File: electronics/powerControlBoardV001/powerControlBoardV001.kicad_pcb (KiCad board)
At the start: 2 copper layers, 2 parts

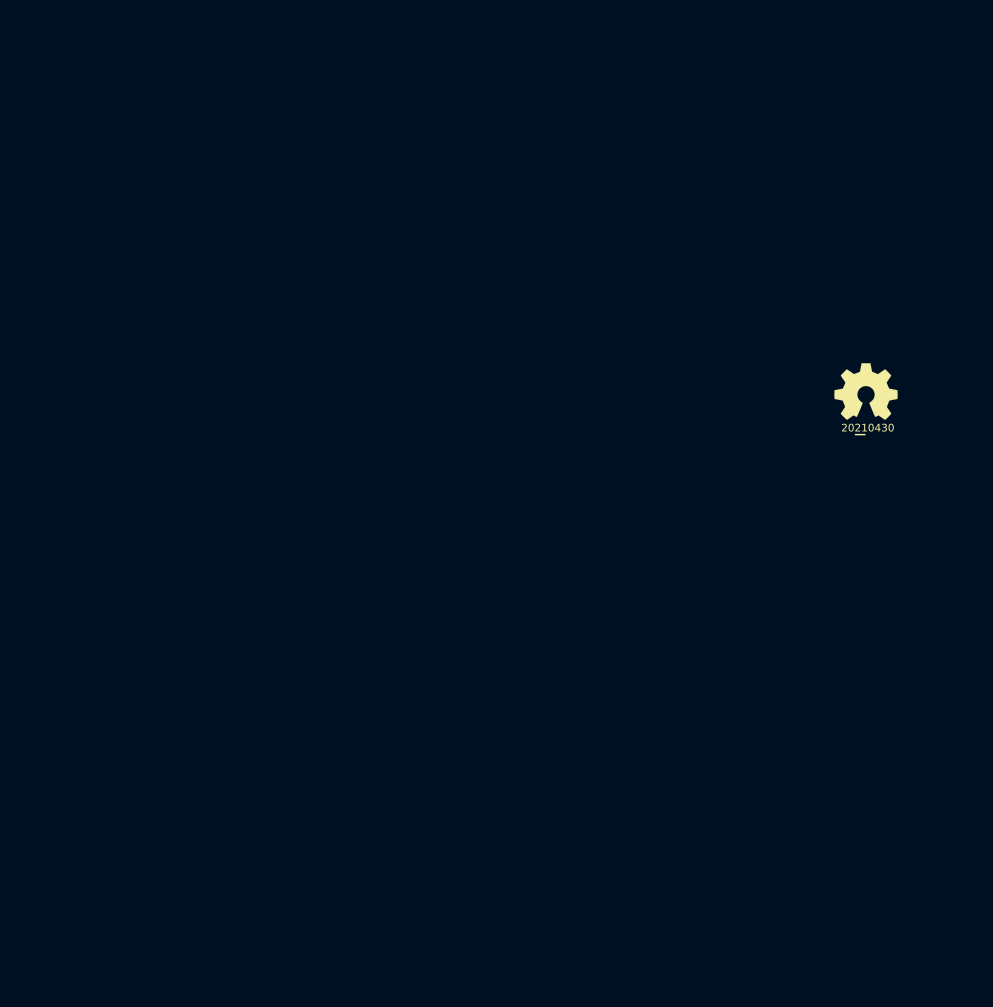
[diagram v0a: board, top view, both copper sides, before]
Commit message: created initial schematic and connections and first PCB outline
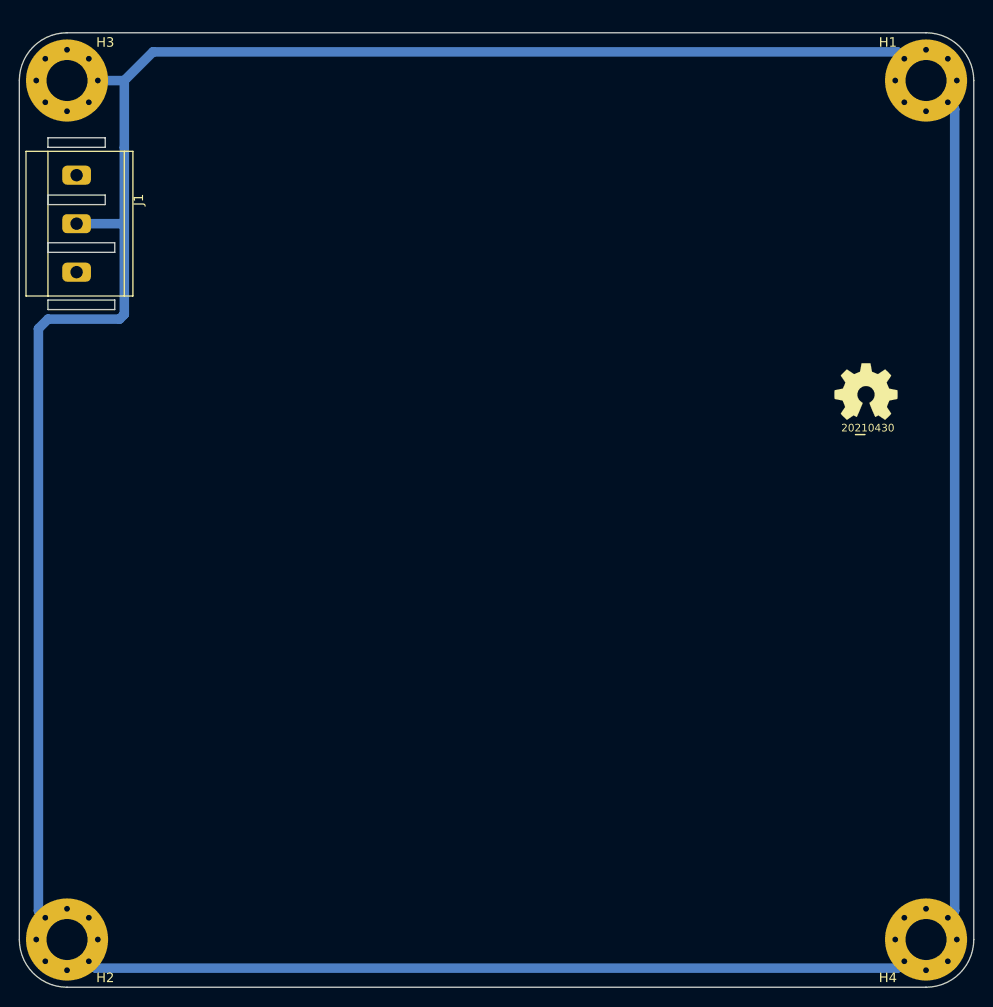
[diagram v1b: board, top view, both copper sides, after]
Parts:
- added H1: M4, MountingHole:MountingHole_4.3mm_M4_Pad_Via, F.Cu at (145.0, 55.0)
- added H2: M4, MountingHole:MountingHole_4.3mm_M4_Pad_Via, F.Cu at (55.0, 145.0)
- added H3: M4, MountingHole:MountingHole_4.3mm_M4_Pad_Via, F.Cu at (55.0, 55.0)
- added H4: M4, MountingHole:MountingHole_4.3mm_M4_Pad_Via, F.Cu at (145.0, 145.0)
- added J1: Conn_01x03, SquantorPhoenixContact:MKDS_3conn_508pitch_1711725, F.Cu at (56.0, 70.0)
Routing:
- net Earth: track 0.00 -> 381.8 mm
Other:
- board outline added: 100 x 100 mm

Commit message: added net filtering parts to PCB, placed, routed, silk optimized
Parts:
- added C201: 4.7n Y2, Capacitor_THT:C_Disc_D10.5mm_W5.0mm_P7.50mm, F.Cu at (84.0, 68.0)
- added C202: 4.7n Y2, Capacitor_THT:C_Disc_D10.5mm_W5.0mm_P7.50mm, F.Cu at (73.0, 68.0)
- added C203: 100n X2, Capacitor_THT:C_Rect_L13.0mm_W6.0mm_P10.00mm_FKS3_FKP3_MKS4, F.Cu at (80.0, 74.0)
- added F201: Fuse, Fuse:Fuseholder_Cylinder-5x20mm_Stelvio-Kontek_PTF78_Horizontal_Open, F.Cu at (87.0, 58.0)
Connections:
- J1 pad 1: /Line -> /Line_in
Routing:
- net /Neutral: track 0.00 -> 42.5 mm
- net Earth: track 381.8 -> 400.7 mm
- net /Line_out: track 0.00 -> 18.9 mm
- net /Line_in: track 0.00 -> 12.8 mm

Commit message: updated versionnumber and cleanup of parts, WIP overall architecture
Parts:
- removed C201, C202: 4.7n Y2, Capacitor_THT:C_Disc_D10.5mm_W5.0mm_P7.50mm
- removed C203: 100n X2, Capacitor_THT:C_Rect_L13.0mm_W6.0mm_P10.00mm_FKS3_FKP3_MKS4
- removed F201: Fuse, Fuse:Fuseholder_Cylinder-5x20mm_Stelvio-Kontek_PTF78_Horizontal_Open
- N1: value 20210430 -> 20220427
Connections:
- J1 pad 1: /Line_in -> /L_in
- J1 pad 3: /Neutral -> /N_in
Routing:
- net Earth: track 400.7 -> 0.00 mm
- net /Neutral: track 42.5 -> 0.00 mm
- net /Line_out: track 18.9 -> 0.00 mm
- net /Line_in: track 12.8 -> 0.00 mm

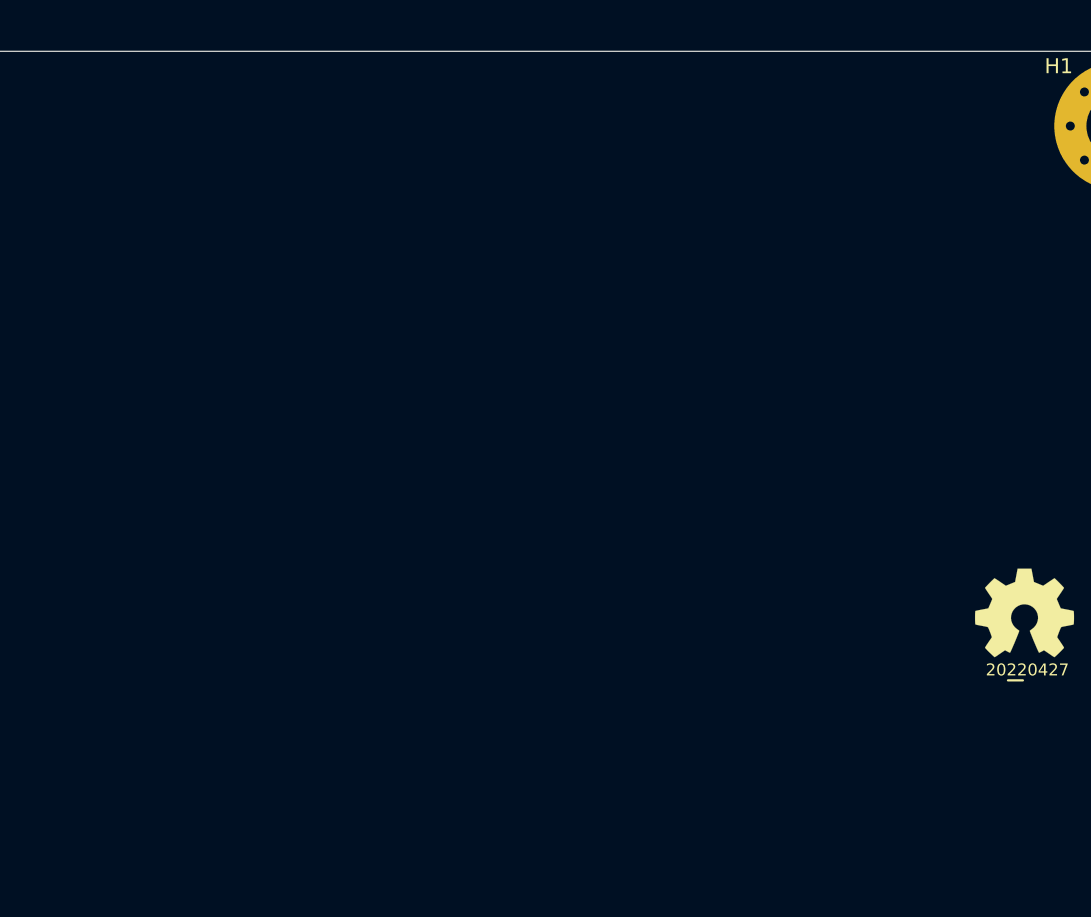
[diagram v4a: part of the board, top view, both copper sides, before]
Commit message: imported initial components into PCB
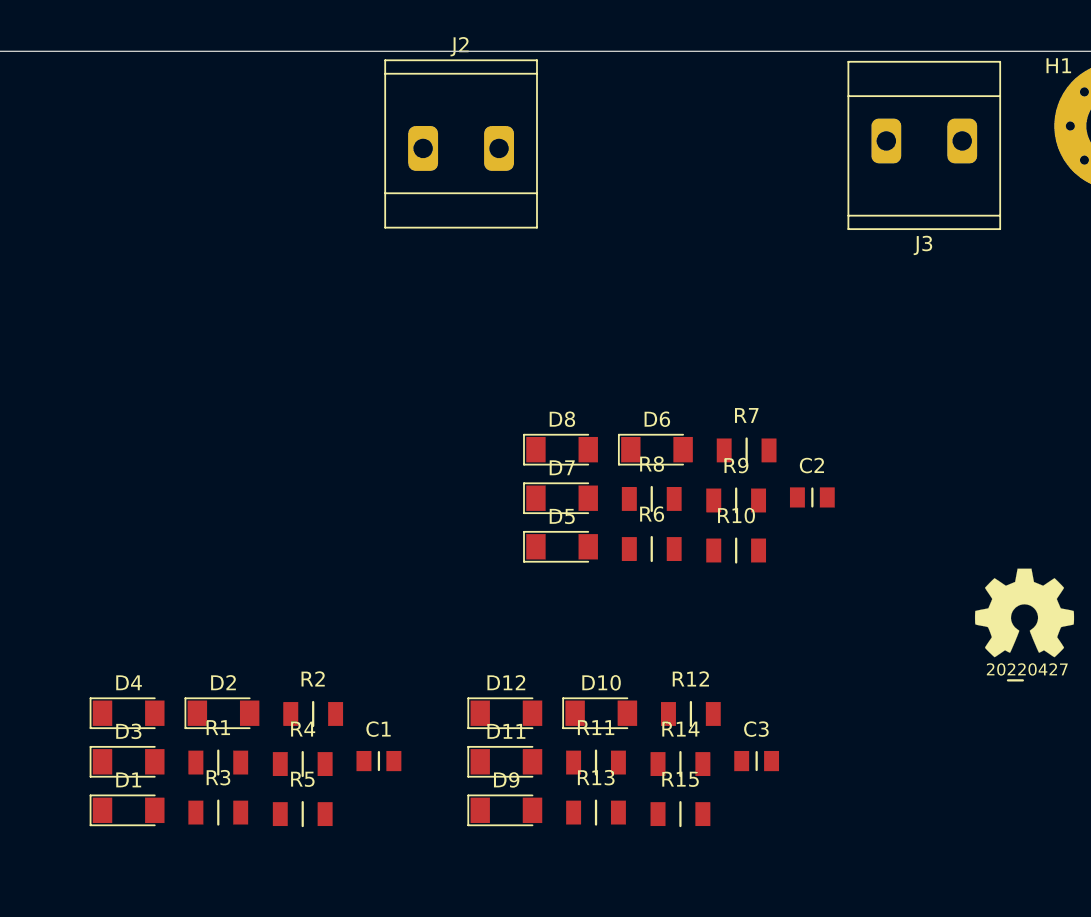
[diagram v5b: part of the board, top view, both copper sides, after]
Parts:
- added C1: 10n, SquantorRcl:C_0805, F.Cu at (95.5, 97.5)
- added C2: 10n, SquantorRcl:C_0805, F.Cu at (124.5, 79.9)
- added C3: 10n, SquantorRcl:C_0805, F.Cu at (120.8, 97.5)
- added D1: 1N4148, Diode_SMD:D_MiniMELF, F.Cu at (78.8, 100.8)
- added D10: 1N4148, Diode_SMD:D_MiniMELF, F.Cu at (110.4, 94.3)
- added D11: 1N4148, Diode_SMD:D_MiniMELF, F.Cu at (104.0, 97.5)
- added D12: 1N4148, Diode_SMD:D_MiniMELF, F.Cu at (104.0, 94.3)
- added D2: 1N4148, Diode_SMD:D_MiniMELF, F.Cu at (85.1, 94.3)
- added D3: 1N4148, Diode_SMD:D_MiniMELF, F.Cu at (78.8, 97.5)
- added D4: 1N4148, Diode_SMD:D_MiniMELF, F.Cu at (78.8, 94.3)
- added D5: 1N4148, Diode_SMD:D_MiniMELF, F.Cu at (107.8, 83.2)
- added D6: 1N4148, Diode_SMD:D_MiniMELF, F.Cu at (114.1, 76.7)
- added D7: 1N4148, Diode_SMD:D_MiniMELF, F.Cu at (107.8, 79.9)
- added D8: 1N4148, Diode_SMD:D_MiniMELF, F.Cu at (107.8, 76.7)
- added D9: 1N4148, Diode_SMD:D_MiniMELF, F.Cu at (104.0, 100.8)
- added J2: Conn_01x02, SquantorPhoenixContact:MKDS_2conn_508pitch_1711725, F.Cu at (101.0, 56.5)
- added J3: Conn_01x02, SquantorPhoenixContact:MKDS_2conn_508pitch_1711725, F.Cu at (132.0, 56.0)
- added R1: 100K, SquantorRcl:C_1206, F.Cu at (84.8, 97.6)
- added R10: 22K, SquantorRcl:C_1206, F.Cu at (119.4, 83.4)
- added R11: 100K, SquantorRcl:C_1206, F.Cu at (110.0, 97.6)
- added R12: 100K, SquantorRcl:C_1206, F.Cu at (116.4, 94.3)
- added R13: 100K, SquantorRcl:C_1206, F.Cu at (110.0, 101.0)
- added R14: 100K, SquantorRcl:C_1206, F.Cu at (115.7, 97.7)
- added R15: 22K, SquantorRcl:C_1206, F.Cu at (115.7, 101.0)
- added R2: 100K, SquantorRcl:C_1206, F.Cu at (91.1, 94.3)
- added R3: 100K, SquantorRcl:C_1206, F.Cu at (84.8, 101.0)
- added R4: 100K, SquantorRcl:C_1206, F.Cu at (90.4, 97.7)
- added R5: 22K, SquantorRcl:C_1206, F.Cu at (90.4, 101.0)
- added R6: 100K, SquantorRcl:C_1206, F.Cu at (113.8, 83.3)
- added R7: 100K, SquantorRcl:C_1206, F.Cu at (120.1, 76.7)
- added R8: 100K, SquantorRcl:C_1206, F.Cu at (113.8, 80.0)
- added R9: 100K, SquantorRcl:C_1206, F.Cu at (119.4, 80.1)

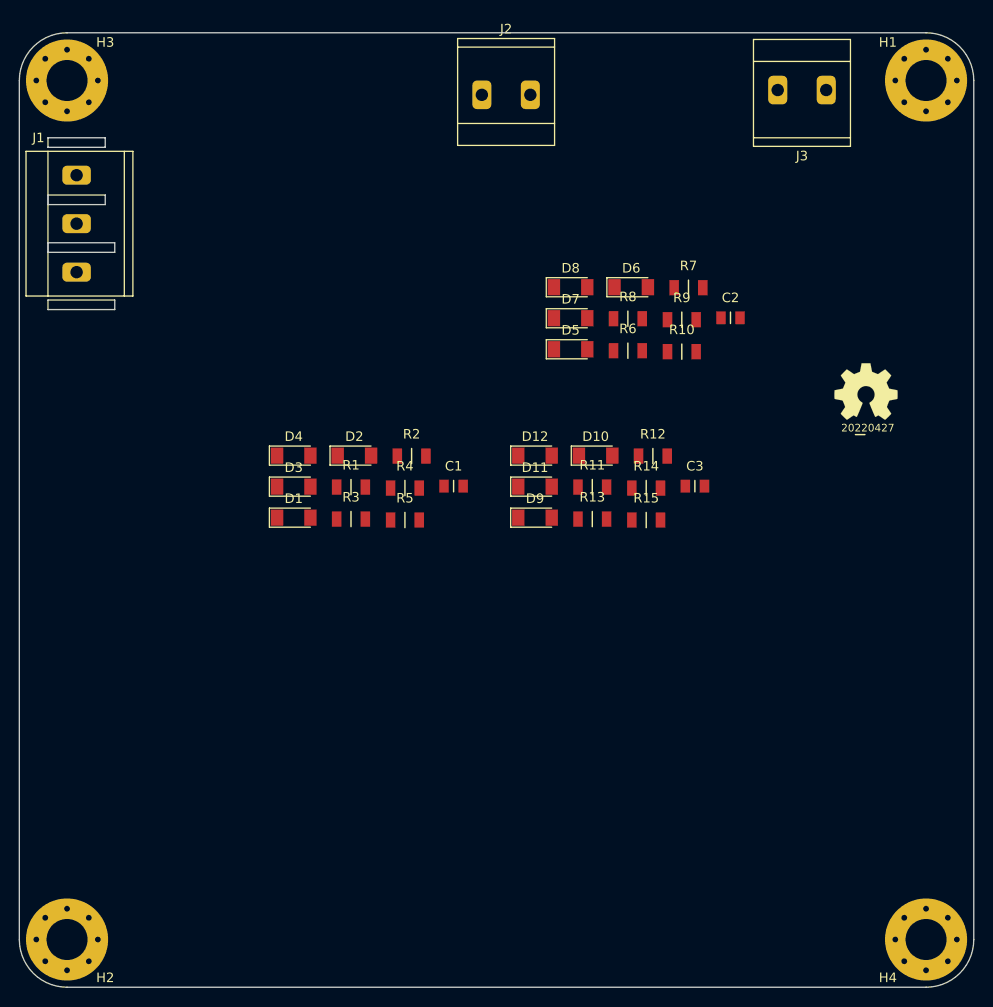
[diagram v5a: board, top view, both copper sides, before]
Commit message: added stuff to board, fixed missing footprint
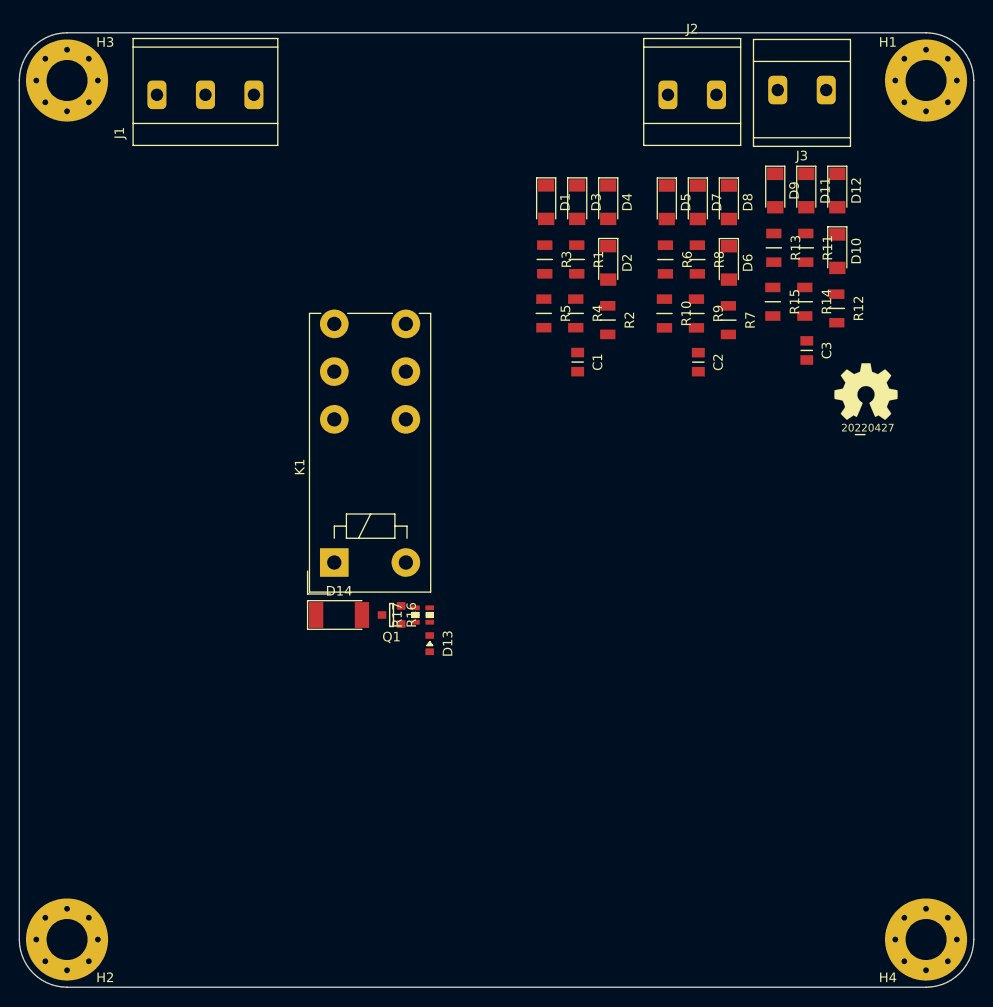
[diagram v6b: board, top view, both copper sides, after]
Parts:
- added D13: LED, SquantorDiodes:LED_0603_hand, F.Cu at (93.0, 114.0)
- added D14: LL4148, Diode_SMD:D_MELF, F.Cu at (83.5, 111.0)
- added K1: FINDER-40.52, Relay_THT:Relay_DPDT_Finder_40.52, F.Cu at (83.0, 105.5)
- added Q1: Q_NMOS_GSD, SquantorIC:SOT23-3, F.Cu at (89.0, 111.0)
- added R16: 1K, SquantorRcl:R_0603, F.Cu at (93.0, 111.0)
- added R17: 10K, SquantorRcl:R_0603, F.Cu at (91.5, 111.0)
- moved D9 42.5 mm to (129.2, 66.5), turned to 270 degrees
- moved D1 42.3 mm to (105.2, 67.8), turned to 270 degrees
- moved D4 42.3 mm to (111.7, 67.8), turned to 270 degrees
- moved D12 42.1 mm to (135.7, 66.5), turned to 270 degrees
- moved D3 42.1 mm to (108.5, 67.8), turned to 270 degrees
- moved D11 42.1 mm to (132.4, 66.5), turned to 270 degrees
- moved R13 34.2 mm to (129.1, 72.5), turned to 270 degrees
- moved R3 33.9 mm to (105.0, 73.8), turned to 270 degrees
- moved R11 33.6 mm to (132.4, 72.5), turned to 270 degrees
- moved R1 33.6 mm to (108.4, 73.8), turned to 270 degrees
- moved D2 33.4 mm to (111.7, 74.1), turned to 270 degrees
- moved D10 33.2 mm to (135.7, 72.9), turned to 270 degrees
- moved R15 26.4 mm to (128.9, 78.2), turned to 270 degrees
- moved R5 26.1 mm to (105.0, 79.4), turned to 270 degrees
- moved R14 25.6 mm to (132.3, 78.2), turned to 270 degrees
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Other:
- outline, holes or cut-outs redrawn
